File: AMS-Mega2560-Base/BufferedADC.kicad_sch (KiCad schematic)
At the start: 9 parts, among them IC6 OPA4340UA

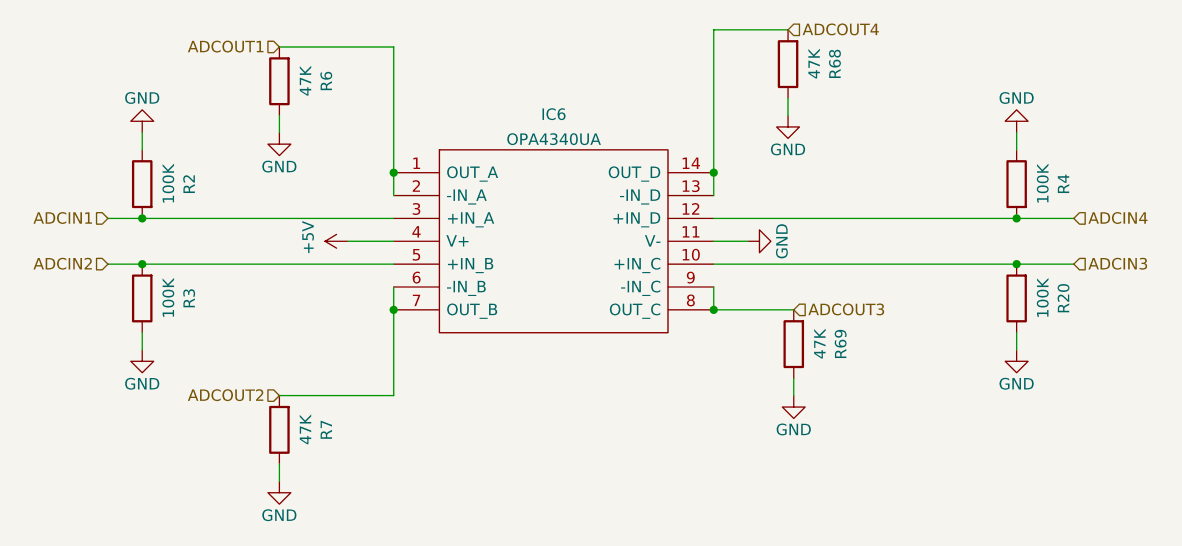
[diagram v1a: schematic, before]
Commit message: updating the inputs and reannotating some stuff.
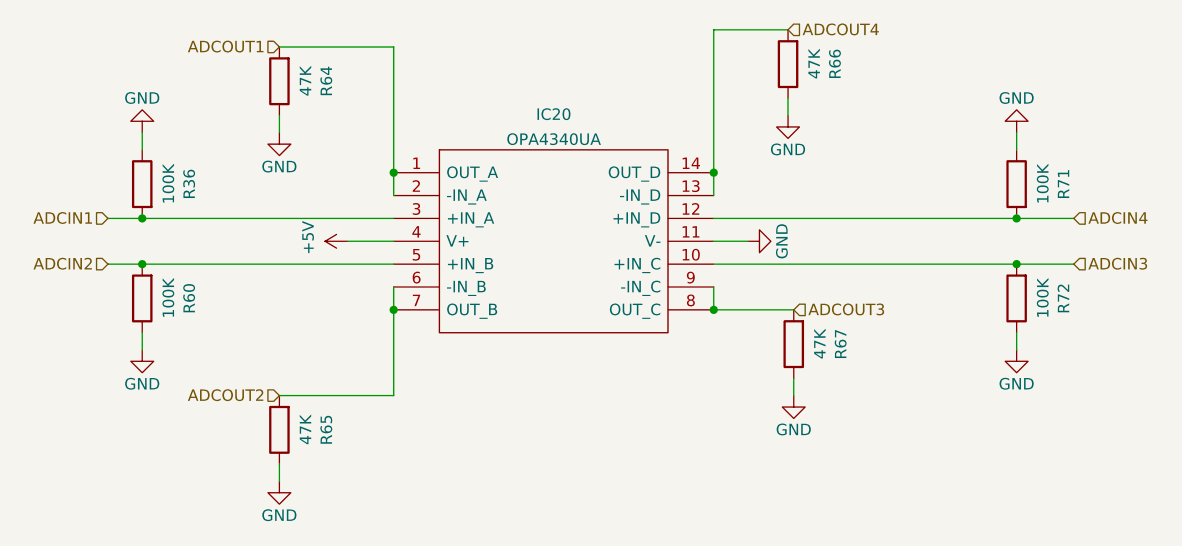
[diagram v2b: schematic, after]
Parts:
- renumbered IC6 to IC20, R2 to R36, R3 to R60, R6 to R64, R7 to R65, R68 to R66, R69 to R67, R4 to R71, R20 to R72
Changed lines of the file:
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@@
   (symbol (lib_id "Device:R") (at 118.745 48.895 180)
     (in_bom yes) (on_board yes)
-    (property "Reference" "R6" (id 0) (at 124.0028 48.895 90))
+    (property "Reference" "R64" (id 0) (at 124.0028 48.895 90))
     (property "Value" "47K" (id 1) (at 121.6914 48.895 90))
     (property "Footprint" "Resistor_THT:R_Axial_DIN0207_L6.3mm_D2.5mm_P2.54mm_Vertical" (id 2) (at 120.523 48.895 90)
@@
   (symbol (lib_id "Samac_Sys:OPA4340UA") (at 131.445 59.055 0)
     (in_bom yes) (on_board yes) (fields_autoplaced)
-    (property "Reference" "IC6" (id 0) (at 149.225 52.5993 0))
+    (property "Reference" "IC20" (id 0) (at 149.225 52.5993 0))
     (property "Value" "OPA4340UA" (id 1) (at 149.225 55.3744 0))
     (property "Footprint" "SOIC127P600X175-14N" (id 2) (at 163.195 56.515 0)
@@
   (symbol (lib_id "Device:R") (at 118.745 87.63 180)
     (in_bom yes) (on_board yes)
-    (property "Reference" "R7" (id 0) (at 124.0028 87.63 90))
+    (property "Reference" "R65" (id 0) (at 124.0028 87.63 90))
     (property "Value" "47K" (id 1) (at 121.6914 87.63 90))
     (property "Footprint" "Resistor_THT:R_Axial_DIN0207_L6.3mm_D2.5mm_P2.54mm_Vertical" (id 2) (at 120.523 87.63 90)
@@
   (symbol (lib_id "Device:R") (at 200.66 73.025 180)
     (in_bom yes) (on_board yes)
-    (property "Reference" "R20" (id 0) (at 205.9178 73.025 90))
+    (property "Reference" "R72" (id 0) (at 205.9178 73.025 90))
     (property "Value" "100K" (id 1) (at 203.6064 73.025 90))
     (property "Footprint" "Resistor_THT:R_Axial_DIN0207_L6.3mm_D2.5mm_P2.54mm_Vertical" (id 2) (at 202.438 73.025 90)
@@
   (symbol (lib_id "Device:R") (at 103.505 60.325 0) (mirror y)
     (in_bom yes) (on_board yes)
-    (property "Reference" "R2" (id 0) (at 108.7628 60.325 90))
+    (property "Reference" "R36" (id 0) (at 108.7628 60.325 90))
     (property "Value" "100K" (id 1) (at 106.4514 60.325 90))
     (property "Footprint" "Resistor_THT:R_Axial_DIN0207_L6.3mm_D2.5mm_P2.54mm_Vertical" (id 2) (at 105.283 60.325 90)
@@
   (symbol (lib_id "Device:R") (at 175.26 46.99 180)
     (in_bom yes) (on_board yes)
-    (property "Reference" "R68" (id 0) (at 180.5178 46.99 90))
+    (property "Reference" "R66" (id 0) (at 180.5178 46.99 90))
     (property "Value" "47K" (id 1) (at 178.2064 46.99 90))
     (property "Footprint" "Resistor_THT:R_Axial_DIN0207_L6.3mm_D2.5mm_P2.54mm_Vertical" (id 2) (at 177.038 46.99 90)
@@
   (symbol (lib_id "Device:R") (at 103.505 73.025 180)
     (in_bom yes) (on_board yes)
-    (property "Reference" "R3" (id 0) (at 108.7628 73.025 90))
+    (property "Reference" "R60" (id 0) (at 108.7628 73.025 90))
     (property "Value" "100K" (id 1) (at 106.4514 73.025 90))
     (property "Footprint" "Resistor_THT:R_Axial_DIN0207_L6.3mm_D2.5mm_P2.54mm_Vertical" (id 2) (at 105.283 73.025 90)
@@
   (symbol (lib_id "Device:R") (at 175.895 78.105 180)
     (in_bom yes) (on_board yes)
-    (property "Reference" "R69" (id 0) (at 181.1528 78.105 90))
+    (property "Reference" "R67" (id 0) (at 181.1528 78.105 90))
     (property "Value" "47K" (id 1) (at 178.8414 78.105 90))
     (property "Footprint" "Resistor_THT:R_Axial_DIN0207_L6.3mm_D2.5mm_P2.54mm_Vertical" (id 2) (at 177.673 78.105 90)
@@
   (symbol (lib_id "Device:R") (at 200.66 60.325 0) (mirror y)
     (in_bom yes) (on_board yes)
-    (property "Reference" "R4" (id 0) (at 205.9178 60.325 90))
+    (property "Reference" "R71" (id 0) (at 205.9178 60.325 90))
     (property "Value" "100K" (id 1) (at 203.6064 60.325 90))
     (property "Footprint" "Resistor_THT:R_Axial_DIN0207_L6.3mm_D2.5mm_P2.54mm_Vertical" (id 2) (at 202.438 60.325 90)
